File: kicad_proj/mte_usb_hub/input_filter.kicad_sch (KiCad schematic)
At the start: 0 parts

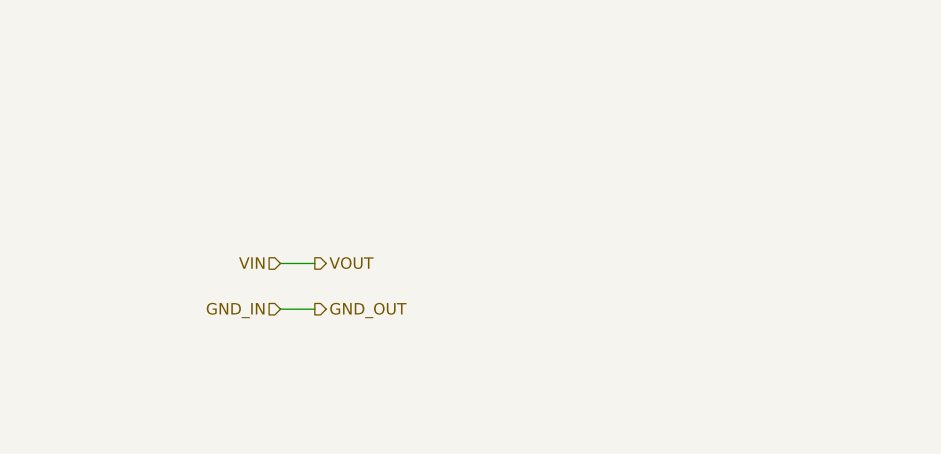
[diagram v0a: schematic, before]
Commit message: Finishes input filter, minor buck changes
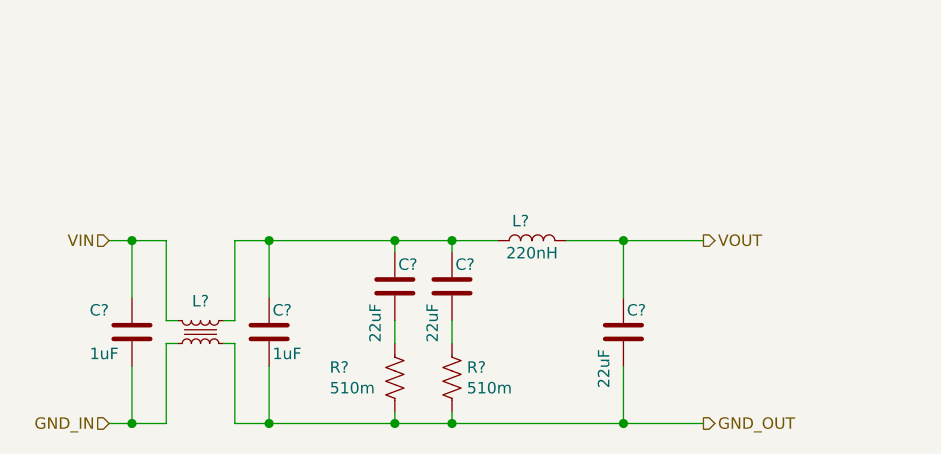
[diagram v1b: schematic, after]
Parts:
- added C? (x3): GCJ32EC71E226KE02, footprints:CAPACITOR_1210N, symbol mte_usb_hub:GCJ32EC71E226KE02
- added C? (x2): CC0603KRX5R9BB105, footprints:CAPACITOR_0603N, symbol mte_usb_hub:CC0603KRX5R9BB105
- added L?: FCUL0624-H-R22M=P3, symbol mte_usb_hub:FCUL0624-H-R22M=P3
- added L?: ACM1211-701-2PL-TL01, footprints:ACM1211-701-2PL-TL01, symbol mte_usb_hub:ACM1211-701-2PL-TL01
- added R? (x2): RL1206JR-070R51L, footprints:RESISTOR_1206N, symbol mte_usb_hub:RL1206JR-070R51L
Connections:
- net GND_IN: now also C?.2, L?.2
- net VIN: now also C?.1, L?.1
- new net: C?.1, C?.1, C?.1, L?.1, L?.4
- new net: C?.2, R?.1 (x2)
- new net GND_OUT: C?.2, C?.2, L?.3, R?.2, R?.2
- new net VOUT: C?.1, L?.2

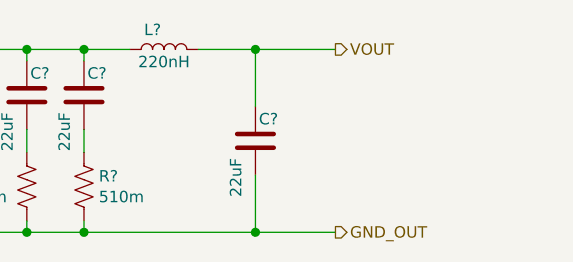
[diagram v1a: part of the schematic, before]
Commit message: Adds bulk capacitors on 12V input
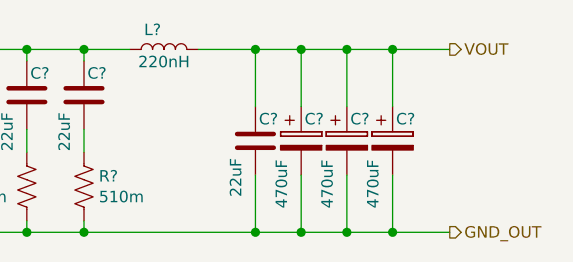
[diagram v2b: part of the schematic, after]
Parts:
- added C? (x3): EEE-HAE471UAP, symbol mte_usb_hub:EEE-HAE471UAP
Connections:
- net GND_OUT: now also C?.2, C?.2, C?.2
- net VOUT: now also C?.1, C?.1, C?.1
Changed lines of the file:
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@@
   (junction (at 127 58.42) (diameter 1.016) (color 0 0 0 0))
   (junction (at 127 78.74) (diameter 1.016) (color 0 0 0 0))
+  (junction (at 132.08 58.42) (diameter 1.016) (color 0 0 0 0))
+  (junction (at 132.08 78.74) (diameter 1.016) (color 0 0 0 0))
+  (junction (at 137.16 58.42) (diameter 1.016) (color 0 0 0 0))
+  (junction (at 137.16 78.74) (diameter 1.016) (color 0 0 0 0))
+  (junction (at 142.24 58.42) (diameter 1.016) (color 0 0 0 0))
+  (junction (at 142.24 78.74) (diameter 1.016) (color 0 0 0 0))
   (wire (pts (xy 72.39 58.42) (xy 69.85 58.42))
     (stroke (width 0) (type solid) (color 0 0 0 0))
@@
     (stroke (width 0) (type solid) (color 0 0 0 0))
   )
-  (wire (pts (xy 127 58.42) (xy 135.89 58.42))
+  (wire (pts (xy 127 58.42) (xy 132.08 58.42))
     (stroke (width 0) (type solid) (color 0 0 0 0))
   )
@@
     (stroke (width 0) (type solid) (color 0 0 0 0))
   )
-  (wire (pts (xy 127 78.74) (xy 135.89 78.74))
+  (wire (pts (xy 127 78.74) (xy 132.08 78.74))
+    (stroke (width 0) (type solid) (color 0 0 0 0))
+  )
+  (wire (pts (xy 132.08 58.42) (xy 132.08 64.77))
+    (stroke (width 0) (type solid) (color 0 0 0 0))
+  )
+  (wire (pts (xy 132.08 58.42) (xy 137.16 58.42))
+    (stroke (width 0) (type solid) (color 0 0 0 0))
+  )
+  (wire (pts (xy 132.08 72.39) (xy 132.08 78.74))
+    (stroke (width 0) (type solid) (color 0 0 0 0))
+  )
+  (wire (pts (xy 132.08 78.74) (xy 137.16 78.74))
+    (stroke (width 0) (type solid) (color 0 0 0 0))
+  )
+  (wire (pts (xy 137.16 58.42) (xy 137.16 64.77))
+    (stroke (width 0) (type solid) (color 0 0 0 0))
+  )
+  (wire (pts (xy 137.16 58.42) (xy 142.24 58.42))
+    (stroke (width 0) (type solid) (color 0 0 0 0))
+  )
+  (wire (pts (xy 137.16 72.39) (xy 137.16 78.74))
+    (stroke (width 0) (type solid) (color 0 0 0 0))
+  )
+  (wire (pts (xy 137.16 78.74) (xy 142.24 78.74))
+    (stroke (width 0) (type solid) (color 0 0 0 0))
+  )
+  (wire (pts (xy 142.24 58.42) (xy 142.24 64.77))
+    (stroke (width 0) (type solid) (color 0 0 0 0))
+  )
+  (wire (pts (xy 142.24 58.42) (xy 148.59 58.42))
+    (stroke (width 0) (type solid) (color 0 0 0 0))
+  )
+  (wire (pts (xy 142.24 72.39) (xy 142.24 78.74))
+    (stroke (width 0) (type solid) (color 0 0 0 0))
+  )
+  (wire (pts (xy 142.24 78.74) (xy 148.59 78.74))
     (stroke (width 0) (type solid) (color 0 0 0 0))
   )
@@
     (effects (font (size 1.27 1.27)) (justify right))
   )
-  (hierarchical_label "VOUT" (shape output) (at 135.89 58.42 0)
+  (hierarchical_label "VOUT" (shape output) (at 148.59 58.42 0)
     (effects (font (size 1.27 1.27)) (justify left))
   )
-  (hierarchical_label "GND_OUT" (shape output) (at 135.89 78.74 0)
+  (hierarchical_label "GND_OUT" (shape output) (at 148.59 78.74 0)
     (effects (font (size 1.27 1.27)) (justify left))
   )
@@
       (effects (font (size 1.27 1.27)) hide)
     )
+    (pin "1")
+    (pin "2")
+  )
+  (symbol (lib_id "mte_usb_hub:EEE-HAE471UAP") (at 132.08 68.58 0) (unit 1)
+    (in_bom yes) (on_board yes)
+    (property "Reference" "C?" (id 0) (at 132.4611 66.1606 0)
+      (effects (font (size 1.27 1.27)) (justify left))
+    )
+    (property "Value" "EEE-HAE471UAP" (id 1) (at 132.715 71.12 0)
+      (effects (font (size 1.27 1.27)) (justify left) hide)
+    )
+    (property "Footprint" "" (id 2) (at 133.0452 72.39 0)
+      (effects (font (size 1.27 1.27)) hide)
+    )
+    (property "Datasheet" "" (id 3) (at 132.08 68.58 0)
+      (effects (font (size 1.27 1.27)) hide)
+    )
+    (property "id" "470uF" (id 4) (at 129.9211 76.0793 90)
+      (effects (font (size 1.27 1.27)) (justify left))
+    )
+    (property "manf" "Panasonic Electronic Components" (id 5) (at 132.08 68.58 0)
+      (effects (font (size 1.27 1.27)) hide)
+    )
+    (pin "1")
+    (pin "2")
+  )
+  (symbol (lib_id "mte_usb_hub:EEE-HAE471UAP") (at 137.16 68.58 0) (unit 1)
+    (in_bom yes) (on_board yes)
+    (property "Reference" "C?" (id 0) (at 137.5411 66.1606 0)
+      (effects (font (size 1.27 1.27)) (justify left))
+    )
+    (property "Value" "EEE-HAE471UAP" (id 1) (at 137.795 71.12 0)
+      (effects (font (size 1.27 1.27)) (justify left) hide)
+    )
+    (property "Footprint" "" (id 2) (at 138.1252 72.39 0)
+      (effects (font (size 1.27 1.27)) hide)
+    )
+    (property "Datasheet" "" (id 3) (at 137.16 68.58 0)
+      (effects (font (size 1.27 1.27)) hide)
+    )
+    (property "id" "470uF" (id 4) (at 135.0011 76.0793 90)
+      (effects (font (size 1.27 1.27)) (justify left))
+    )
+    (property "manf" "Panasonic Electronic Components" (id 5) (at 137.16 68.58 0)
+      (effects (font (size 1.27 1.27)) hide)
+    )
+    (pin "1")
+    (pin "2")
+  )
+  (symbol (lib_id "mte_usb_hub:EEE-HAE471UAP") (at 142.24 68.58 0) (unit 1)
+    (in_bom yes) (on_board yes)
+    (property "Reference" "C?" (id 0) (at 142.6211 66.1606 0)
+      (effects (font (size 1.27 1.27)) (justify left))
+    )
+    (property "Value" "EEE-HAE471UAP" (id 1) (at 142.875 71.12 0)
+      (effects (font (size 1.27 1.27)) (justify left) hide)
+    )
+    (property "Footprint" "" (id 2) (at 143.2052 72.39 0)
+      (effects (font (size 1.27 1.27)) hide)
+    )
+    (property "Datasheet" "" (id 3) (at 142.24 68.58 0)
+      (effects (font (size 1.27 1.27)) hide)
+    )
+    (property "id" "470uF" (id 4) (at 140.0811 76.0793 90)
+      (effects (font (size 1.27 1.27)) (justify left))
+    )
+    (property "manf" "Panasonic Electronic Components" (id 5) (at 142.24 68.58 0)
+      (effects (font (size 1.27 1.27)) hide)
+    )

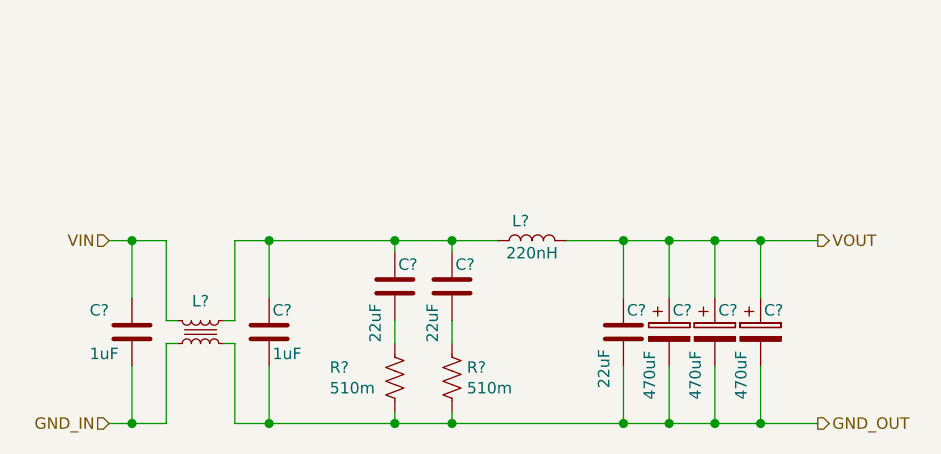
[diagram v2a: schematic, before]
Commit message: Updates input protection, output BC enabled
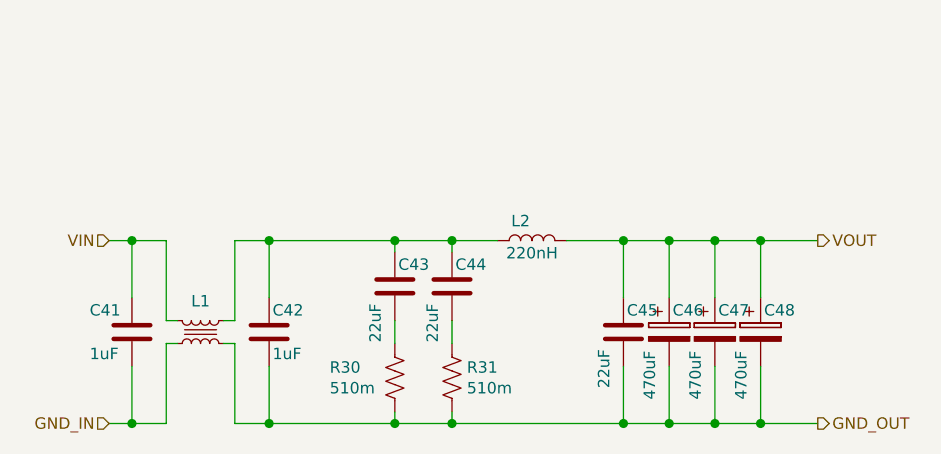
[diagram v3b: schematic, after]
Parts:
- gave numbers to parts that had none: 12
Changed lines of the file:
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@@
-(kicad_sch (version 20210126) (generator eeschema)
+(kicad_sch (version 20210406) (generator eeschema)
   (paper "A4")
   (junction (at 72.39 58.42) (diameter 1.016) (color 0 0 0 0))
@@
   (symbol (lib_id "mte_usb_hub:FCUL0624-H-R22M=P3") (at 116.84 58.42 90) (unit 1)
     (in_bom yes) (on_board yes)
-    (property "Reference" "L?" (id 0) (at 115.57 56.2418 90))
+    (property "Reference" "L2" (id 0) (at 115.57 56.2418 90))
     (property "Value" "FCUL0624-H-R22M=P3" (id 1) (at 116.84 56.515 90)
       (effects (font (size 1.27 1.27)) hide)
@@
   (symbol (lib_id "mte_usb_hub:RL1206JR-070R51L") (at 101.6 73.66 0) (unit 1)
     (in_bom yes) (on_board yes)
-    (property "Reference" "R?" (id 0) (at 94.3611 72.5106 0)
+    (property "Reference" "R30" (id 0) (at 94.3611 72.5106 0)
       (effects (font (size 1.27 1.27)) (justify left))
     )
@@
   (symbol (lib_id "mte_usb_hub:RL1206JR-070R51L") (at 107.95 73.66 0) (unit 1)
     (in_bom yes) (on_board yes)
-    (property "Reference" "R?" (id 0) (at 109.6011 72.5106 0)
+    (property "Reference" "R31" (id 0) (at 109.6011 72.5106 0)
       (effects (font (size 1.27 1.27)) (justify left))
     )
@@
   (symbol (lib_id "mte_usb_hub:ACM1211-701-2PL-TL01") (at 80.01 68.58 0) (unit 1)
     (in_bom yes) (on_board yes)
-    (property "Reference" "L?" (id 0) (at 80.01 65.1446 0))
+    (property "Reference" "L1" (id 0) (at 80.01 65.1446 0))
     (property "Value" "ACM1211-701-2PL-TL01" (id 1) (at 80.01 71.755 0)
       (effects (font (size 1.27 1.27)) hide)
@@
   (symbol (lib_id "mte_usb_hub:CC0603KRX5R9BB105") (at 72.39 68.58 0) (unit 1)
     (in_bom yes) (on_board yes)
-    (property "Reference" "C?" (id 0) (at 67.6911 66.1606 0)
+    (property "Reference" "C41" (id 0) (at 67.6911 66.1606 0)
       (effects (font (size 1.27 1.27)) (justify left))
     )
@@
   (symbol (lib_id "mte_usb_hub:CC0603KRX5R9BB105") (at 87.63 68.58 0) (unit 1)
     (in_bom yes) (on_board yes)
-    (property "Reference" "C?" (id 0) (at 88.0111 66.1606 0)
+    (property "Reference" "C42" (id 0) (at 88.0111 66.1606 0)
       (effects (font (size 1.27 1.27)) (justify left))
     )
@@
   (symbol (lib_id "mte_usb_hub:GCJ32EC71E226KE02") (at 101.6 63.5 0) (unit 1)
     (in_bom yes) (on_board yes)
-    (property "Reference" "C?" (id 0) (at 101.9811 61.0806 0)
+    (property "Reference" "C43" (id 0) (at 101.9811 61.0806 0)
       (effects (font (size 1.27 1.27)) (justify left))
     )
@@
   (symbol (lib_id "mte_usb_hub:GCJ32EC71E226KE02") (at 107.95 63.5 0) (unit 1)
     (in_bom yes) (on_board yes)
-    (property "Reference" "C?" (id 0) (at 108.3311 61.0806 0)
+    (property "Reference" "C44" (id 0) (at 108.3311 61.0806 0)
       (effects (font (size 1.27 1.27)) (justify left))
     )
@@
   (symbol (lib_id "mte_usb_hub:GCJ32EC71E226KE02") (at 127 68.58 0) (unit 1)
     (in_bom yes) (on_board yes)
-    (property "Reference" "C?" (id 0) (at 127.3811 66.1606 0)
+    (property "Reference" "C45" (id 0) (at 127.3811 66.1606 0)
       (effects (font (size 1.27 1.27)) (justify left))
     )
@@
   (symbol (lib_id "mte_usb_hub:EEE-HAE471UAP") (at 132.08 68.58 0) (unit 1)
     (in_bom yes) (on_board yes)
-    (property "Reference" "C?" (id 0) (at 132.4611 66.1606 0)
+    (property "Reference" "C46" (id 0) (at 132.4611 66.1606 0)
       (effects (font (size 1.27 1.27)) (justify left))
     )
@@
   (symbol (lib_id "mte_usb_hub:EEE-HAE471UAP") (at 137.16 68.58 0) (unit 1)
     (in_bom yes) (on_board yes)
-    (property "Reference" "C?" (id 0) (at 137.5411 66.1606 0)
+    (property "Reference" "C47" (id 0) (at 137.5411 66.1606 0)
       (effects (font (size 1.27 1.27)) (justify left))
     )
@@
   (symbol (lib_id "mte_usb_hub:EEE-HAE471UAP") (at 142.24 68.58 0) (unit 1)
     (in_bom yes) (on_board yes)
-    (property "Reference" "C?" (id 0) (at 142.6211 66.1606 0)
-      (effects (font (size 1.27 1.27)) (justify left))
-    )
+    (property "Reference" "C48" (id 0) (at 142.6211 66.1606 0)
+      (effects (font (size 1.27 1.27)) (justify left))
+    )

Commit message: New changes from the livestream
Starts the layout
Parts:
- removed C48: EEE-HAE471UAP, symbol mte_usb_hub:EEE-HAE471UAP
- removed R31: RL1206JR-070R51L, footprints:RESISTOR_1206N, symbol mte_usb_hub:RL1206JR-070R51L
- added C48: GCJ32EC71E226KE02, mte_usb_footprints:CAPACITOR_1210N, symbol mte_usb_hub:GCJ32EC71E226KE02
- C41, C42: footprint footprints:CAPACITOR_0603N -> mte_usb_footprints:CAPACITOR_0603N
- C43, C44, C45: footprint footprints:CAPACITOR_1210N -> mte_usb_footprints:CAPACITOR_1210N
- C46, C47: footprint (none) -> mte_usb_footprints:CAPAE1030X1080L350X120N
- L1: footprint footprints:ACM1211-701-2PL-TL01 -> mte_usb_footprints:ACM1211-701-2PL-TL01
- L2: footprint (none) -> mte_usb_footprints:INDM730X660X240L150X140N
- R30: footprint footprints:RESISTOR_1206N -> mte_usb_footprints:RESISTOR_1206N
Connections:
- net GND_OUT: now also C43.2, C44.2
- net at C42.1, C43.1, C44.1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: now also C48.1
- net at R30.1: now also C48.2; no longer C43.2
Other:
- note added: "Max total input transient current, I_{in} = 5A Total bulk capacitance required C = (1.21 * I_{in}^{2} * L) / V^{2} C = (1.21 * 5^{2} * (220 * 10^{-9}) / 0.1^{2} C = 665.5uF"
